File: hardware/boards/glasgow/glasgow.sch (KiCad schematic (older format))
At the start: 93 parts, among them J1 USB_B_Micro, U1 CY7C68013A-56LTX, U15 TPD3S014, U2 CAT24M01W, U3 CAT24C256W, U30 ICE40HX8K-BG121, U34 ATECC508A, U36 TLV75533PDRVR, U7 LM3880MF-1AF, U8 TLV73312PQDRVRQ1, Y1 24M

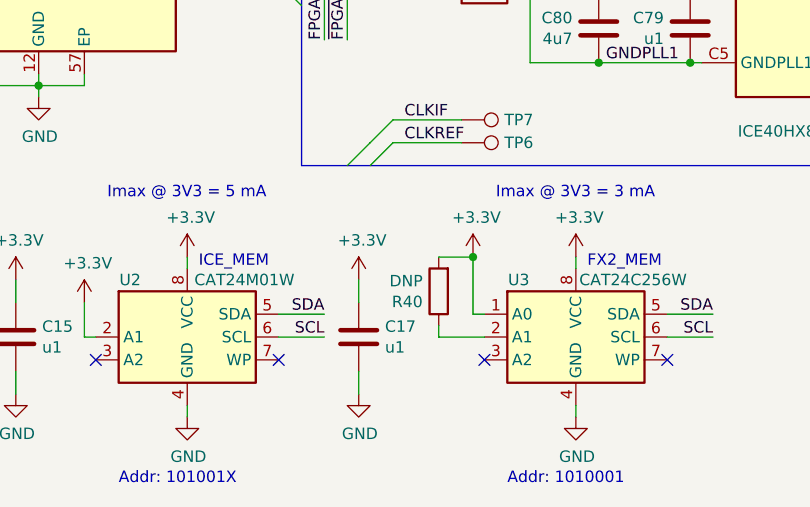
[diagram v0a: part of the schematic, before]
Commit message: revC1: remove DNP part models & add DNP field in sch
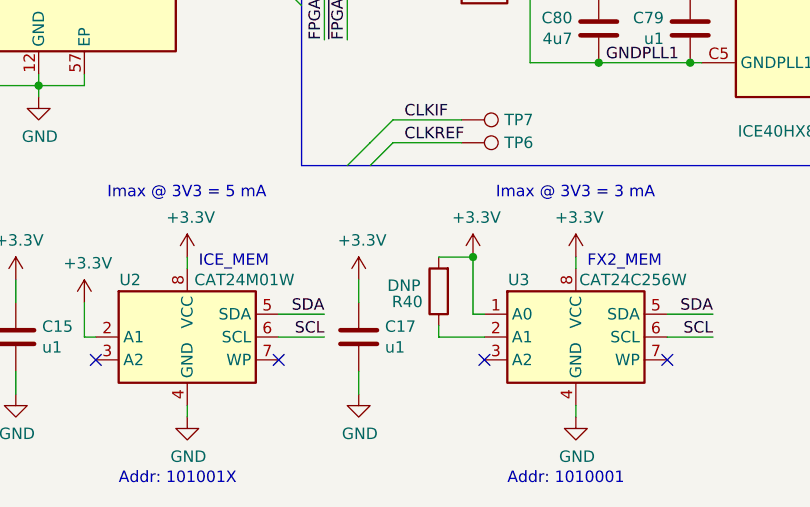
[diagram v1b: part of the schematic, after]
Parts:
- R40: DNP (none) -> DNP
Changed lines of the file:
@@
 P 5300 6800
 F 0 "R40" H 5370 6846 50  0000 L CNN
-F 1 "DNP" H 5370 6755 50  0000 L CNN
+F 1 "DNP" H 5370 6755 50  0001 L CNN
 F 2 "Resistor_SMD:R_0402_1005Metric" V 5230 6800 50  0001 C CNN
-F 3 "https://www.mouser.com/datasheet/2/447/PYu-RC_Group_51_RoHS_L_9-1314892.pdf" H 5300 6800 50  0001 C CNN
+F 3 "" H 5300 6800 50  0001 C CNN
+F 4 "DNP" H 5525 6775 50  0000 R CNN "DNP"
 	1    5300 6800
 	-1   0    0    1

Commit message: revC1: Updated BOM management keys in the schematic.
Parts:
- C87: 1b2-bom-key (none) -> cap-elec-5x3_9-150u
- U36: 1b2-bom-key (none) -> ic-dfn6-tlv75533pdrvr
- U8: 1b2-bom-key (none) -> ic-dfn6-tlv73312pqrdvrq1
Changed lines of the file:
@@
 F 2 "Glasgow:DFN-6-1EP_2x2mm_P0.65mm_EP1x1.6mm_ThermalVias" H 9800 5075 50  0001 C CIN
 F 3 "http://www.ti.com/lit/ds/symlink/tlv733p-q1.pdf" H 9800 4800 50  0001 C CNN
+F 4 "ic-dfn6-tlv73312pqrdvrq1" H 9800 4750 50  0001 C CNN "1b2-bom-key"
 	1    9800 4750
 	1    0    0    -1
@@
 F 2 "Glasgow:DFN-6-1EP_2x2mm_P0.65mm_EP1x1.6mm_ThermalVias" H 9800 6125 50  0001 C CIN
 F 3 "http://www.ti.com/lit/ds/symlink/tlv755p.pdf" H 9800 5850 50  0001 C CNN
+F 4 "ic-dfn6-tlv75533pdrvr" H 9800 5800 50  0001 C CNN "1b2-bom-key"
 	1    9800 5800
 	1    0    0    -1
@@
 F 4 "APXF6R3ARA151ME40G" H 8200 5050 50  0001 C CNN "MPN"
 F 5 "United Chemi-Con" H 8200 5050 50  0001 C CNN "Mfg"
+F 6 "cap-elec-5x3_9-150u" H 8200 5050 50  0001 C CNN "1b2-bom-key"
 	1    8200 5050
 	1    0    0    -1

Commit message: revC1: change bulk decoupling cap to polymer in 1b2 key
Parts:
- C87: 1b2-bom-key cap-elec-5x3_9-150u -> cap-poly-5x3_9-150u
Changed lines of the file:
@@
 F 4 "APXF6R3ARA151ME40G" H 8200 5050 50  0001 C CNN "MPN"
 F 5 "United Chemi-Con" H 8200 5050 50  0001 C CNN "Mfg"
-F 6 "cap-elec-5x3_9-150u" H 8200 5050 50  0001 C CNN "1b2-bom-key"
+F 6 "cap-poly-5x3_9-150u" H 8200 5050 50  0001 C CNN "1b2-bom-key"
 	1    8200 5050
 	1    0    0    -1

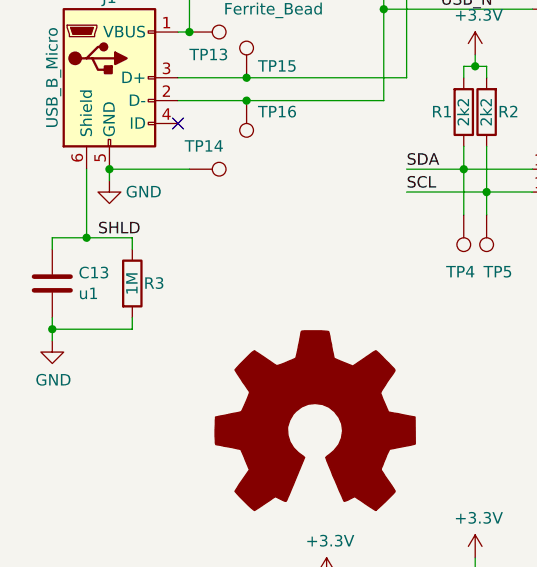
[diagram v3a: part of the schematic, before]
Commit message: revC1: reduce count of different resistor values
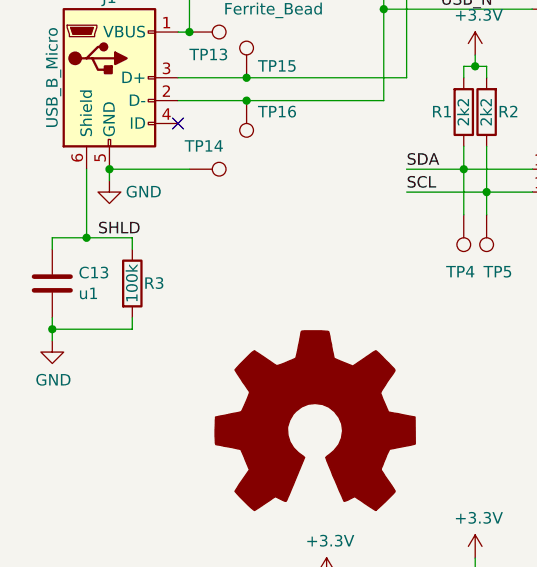
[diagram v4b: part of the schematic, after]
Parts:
- R3: value 1M -> 100k; 1b2-bom-key res-0402-1m -> res-0402-100k; MPN RC0402FR-131ML -> RC0402FR-13100KL
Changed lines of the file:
@@
 P 1100 5450
 F 0 "R3" H 1150 5450 50  0000 L CNN
-F 1 "1M" V 1100 5450 50  0000 C CNN
+F 1 "100k" V 1100 5450 50  0000 C CNN
 F 2 "Resistor_SMD:R_0402_1005Metric" V 1030 5450 50  0001 C CNN
 F 3 "https://www.mouser.com/datasheet/2/447/PYu-RC_Group_51_RoHS_L_10-1527934.pdf" H 1100 5450 50  0001 C CNN
 F 4 "Yageo" H -50 400 50  0001 C CNN "Mfg"
-F 5 "RC0402FR-131ML" H -50 400 50  0001 C CNN "MPN"
-F 6 "res-0402-1m" H 1100 5450 50  0001 C CNN "1b2-bom-key"
+F 5 "RC0402FR-13100KL" H -50 400 50  0001 C CNN "MPN"
+F 6 "res-0402-100k" H 1100 5450 50  0001 C CNN "1b2-bom-key"
 	1    1100 5450
 	1    0    0    -1

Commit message: RevC1: Added missing component MPN/Mfg values
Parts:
- U30: MPN (none) -> ICE40HX8K-BG121; Mfg (none) -> Lattice Semiconductor Corporation
- U34: MPN ATECC508A -> ATECC508A-MAHDA-T
- U36: MPN (none) -> TLV75533PDRVR; Mfg (none) -> Texas Instruments
- U8: MPN (none) -> TLV73312PQDRVRQ1; Mfg (none) -> Texas Instruments
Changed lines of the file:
@@
 F 3 "http://www.latticesemi.com/Products/FPGAandCPLD/iCE40" H 5950 4150 50  0001 C CNN
 F 4 "ic-ice40hx8k-bg121" H 6800 3150 50  0001 C CNN "1b2-bom-key"
+F 5 "ICE40HX8K-BG121" H 6800 3150 50  0001 C CNN "MPN"
+F 6 "Lattice Semiconductor Corporation" H 6800 3150 50  0001 C CNN "Mfg"
 	3    6800 3150
 	-1   0    0    -1
@@
 F 3 "http://www.latticesemi.com/Products/FPGAandCPLD/iCE40" H 6200 6400 50  0001 C CNN
 F 4 "ic-ice40hx8k-bg121" H 7050 5400 50  0001 C CNN "1b2-bom-key"
+F 5 "ICE40HX8K-BG121" H 7050 5400 50  0001 C CNN "MPN"
+F 6 "Lattice Semiconductor Corporation" H 7050 5400 50  0001 C CNN "Mfg"
 	5    7050 5400
 	-1   0    0    -1
@@
 F 3 "http://ww1.microchip.com/downloads/en/DeviceDoc/20005927A.pdf" H 2600 7000 50  0001 C CNN
 F 4 "Microchip" H 2600 7000 50  0001 C CNN "Mfg"
-F 5 "ATECC508A" H 2600 7000 50  0001 C CNN "MPN"
+F 5 "ATECC508A-MAHDA-T" H 2600 7000 50  0001 C CNN "MPN"
 F 6 "ic-wdfn8-atecc508a" H 2600 7000 50  0001 C CNN "1b2-bom-key"
 	1    2600 7000
@@
 F 3 "http://www.ti.com/lit/ds/symlink/tlv733p-q1.pdf" H 9800 4800 50  0001 C CNN
 F 4 "ic-dfn6-tlv73312pqrdvrq1" H 9800 4750 50  0001 C CNN "1b2-bom-key"
+F 5 "TLV73312PQDRVRQ1" H 9800 4750 50  0001 C CNN "MPN"
+F 6 "Texas Instruments" H 9800 4750 50  0001 C CNN "Mfg"
 	1    9800 4750
 	1    0    0    -1
@@
 F 3 "http://www.ti.com/lit/ds/symlink/tlv755p.pdf" H 9800 5850 50  0001 C CNN
 F 4 "ic-dfn6-tlv75533pdrvr" H 9800 5800 50  0001 C CNN "1b2-bom-key"
+F 5 "TLV75533PDRVR" H 9800 5800 50  0001 C CNN "MPN"
+F 6 "Texas Instruments" H 9800 5800 50  0001 C CNN "Mfg"
 	1    9800 5800
 	1    0    0    -1

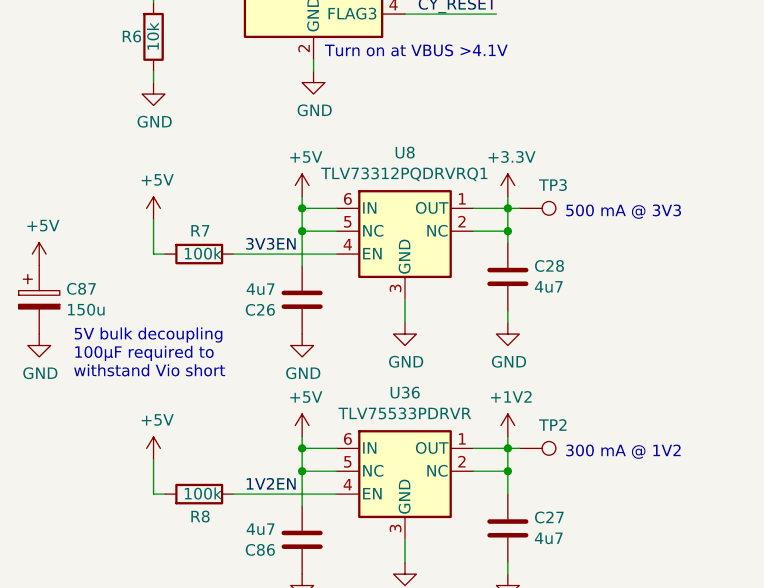
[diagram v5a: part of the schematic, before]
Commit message: revC1: Swap miss labelled 1V2/3V3 regulator MPNs
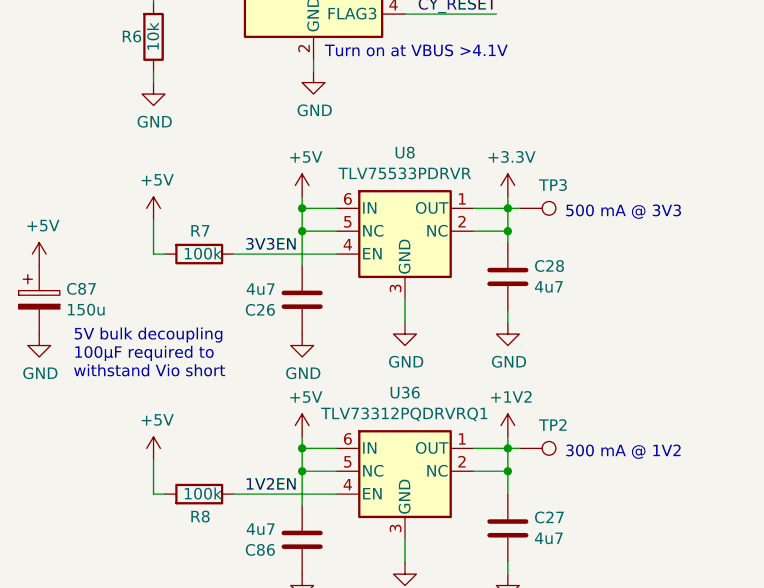
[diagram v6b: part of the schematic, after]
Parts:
- U36: value TLV75533PDRVR -> TLV73312PQDRVRQ1; 1b2-bom-key ic-dfn6-tlv75533pdrvr -> ic-dfn6-tlv73312pqrdvrq1; MPN TLV75533PDRVR -> TLV73312PQDRVRQ1
- U8: value TLV73312PQDRVRQ1 -> TLV75533PDRVR; 1b2-bom-key ic-dfn6-tlv73312pqrdvrq1 -> ic-dfn6-tlv75533pdrvr; MPN TLV73312PQDRVRQ1 -> TLV75533PDRVR
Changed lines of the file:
@@
 P 9800 4750
 F 0 "U8" H 9800 5092 50  0000 C CNN
-F 1 "TLV73312PQDRVRQ1" H 9800 5001 50  0000 C CNN
+F 1 "TLV75533PDRVR" H 9800 5001 50  0000 C CNN
 F 2 "Glasgow:DFN-6-1EP_2x2mm_P0.65mm_EP1x1.6mm_ThermalVias" H 9800 5075 50  0001 C CIN
 F 3 "http://www.ti.com/lit/ds/symlink/tlv733p-q1.pdf" H 9800 4800 50  0001 C CNN
-F 4 "ic-dfn6-tlv73312pqrdvrq1" H 9800 4750 50  0001 C CNN "1b2-bom-key"
-F 5 "TLV73312PQDRVRQ1" H 9800 4750 50  0001 C CNN "MPN"
+F 4 "ic-dfn6-tlv75533pdrvr" H 9800 4750 50  0001 C CNN "1b2-bom-key"
+F 5 "TLV75533PDRVR" H 9800 4750 50  0001 C CNN "MPN"
 F 6 "Texas Instruments" H 9800 4750 50  0001 C CNN "Mfg"
 	1    9800 4750
@@
 P 9800 5800
 F 0 "U36" H 9800 6142 50  0000 C CNN
-F 1 "TLV75533PDRVR" H 9800 6051 50  0000 C CNN
+F 1 "TLV73312PQDRVRQ1" H 9800 6051 50  0000 C CNN
 F 2 "Glasgow:DFN-6-1EP_2x2mm_P0.65mm_EP1x1.6mm_ThermalVias" H 9800 6125 50  0001 C CIN
 F 3 "http://www.ti.com/lit/ds/symlink/tlv755p.pdf" H 9800 5850 50  0001 C CNN
-F 4 "ic-dfn6-tlv75533pdrvr" H 9800 5800 50  0001 C CNN "1b2-bom-key"
-F 5 "TLV75533PDRVR" H 9800 5800 50  0001 C CNN "MPN"
+F 4 "ic-dfn6-tlv73312pqrdvrq1" H 9800 5800 50  0001 C CNN "1b2-bom-key"
+F 5 "TLV73312PQDRVRQ1" H 9800 5800 50  0001 C CNN "MPN"
 F 6 "Texas Instruments" H 9800 5800 50  0001 C CNN "Mfg"
 	1    9800 5800

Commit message: revC1: swap regulator library references
This was missed in f1772ca
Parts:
- U36: symbol Glasgow:TLV75533PDRVR -> Glasgow:TLV73312PQDRVRQ1
- U8: symbol Glasgow:TLV73312PQDRVRQ1 -> Glasgow:TLV75533PDRVR
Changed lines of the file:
@@
 $EndComp
 $Comp
-L Glasgow:TLV73312PQDRVRQ1 U8
+L Glasgow:TLV75533PDRVR U8
 U 1 1 5CEC297B
 P 9800 4750
@@
 $EndComp
 $Comp
-L Glasgow:TLV75533PDRVR U36
+L Glasgow:TLV73312PQDRVRQ1 U36
 U 1 1 5CEC599A
 P 9800 5800

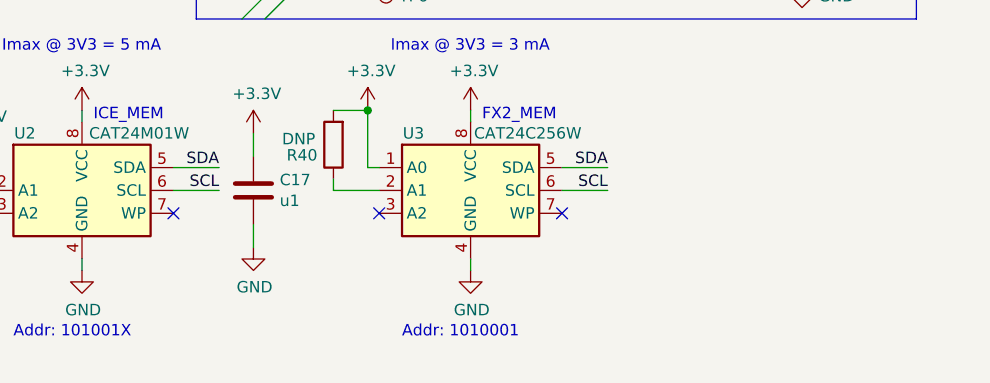
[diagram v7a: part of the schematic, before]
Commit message: hardware/boards/glasgow: explain the function of R40.
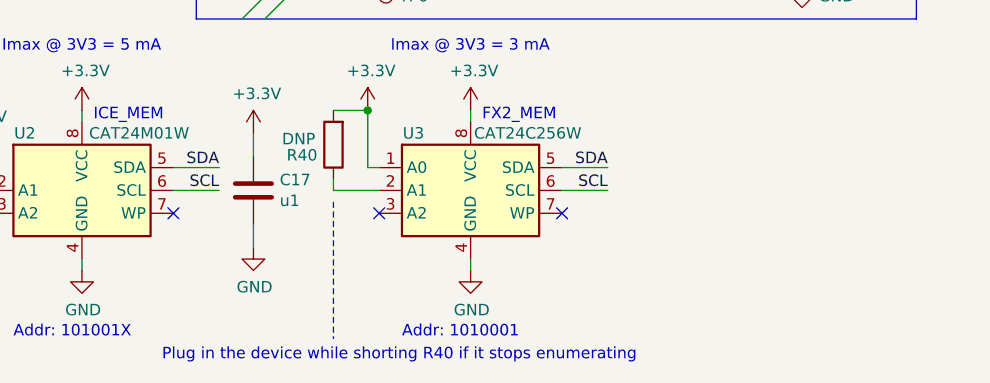
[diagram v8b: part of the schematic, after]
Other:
- note added: "Plug in the device while shorting R40 if it stops enumerating"
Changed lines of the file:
@@
-EESchema Schematic File Version 4
-LIBS:glasgow-cache
-EELAYER 29 0
+EESchema Schematic File Version 5
+EELAYER 30 0
 EELAYER END
 $Descr A4 11693 8268
@@
 Comment3 ""
 Comment4 ""
+Comment5 ""
+Comment6 ""
+Comment7 ""
+Comment8 ""
+Comment9 ""
 $EndDescr
 $Comp
@@
 Wire Wire Line
 	2300 3700 2300 4150
+Wire Notes Line
+	5300 7050 5300 7650
+Text Notes 4550 7750 0    50   ~ 0
+Plug in the device while shorting R40 if it stops enumerating
 Wire Bus Line
 	4700 6250 7850 6250
